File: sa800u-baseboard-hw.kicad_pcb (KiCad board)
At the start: 2 copper layers, 100 x 68 mm, 169 parts, among them IC1 TPS2378DDA, J1 WE-RJ45_7499111121A, J10 2908-05WB-MG, J11 MC-HVT1-S04-G, J12 MC-HVT1-S04-G, J13 MC-HVT1-S04-G, J14 MC-HVT1-S04-G, J2 46756-1001, J4 WE_632723300011, J5 WE_632723300011, J6 WE_632723300011, J7 3-84952-0, J8 F52R-1A7H1-11020, J9 WE_68715014522, Q1 2N7000, Q2 2N7000, Q3 2N7000, T1 749020010A, U1 RTL8111H, U10 MDT580M01001, U11 AP62301Z6-7, U12 AP62301Z6-7, U13 TPS65982BB, U2 LT9611, U3 TXB0104RUT, U4 TXS0102YZPR, U5 TS3USB30EDGSR, U6 FT2232HL-REEL, U7 USB57442G, U8 SA800U-WF, U9 MAX13042EEBC+T, Y1 ECS-1618-250-BN-TR, Y2 ECS-1618-250-BN-TR

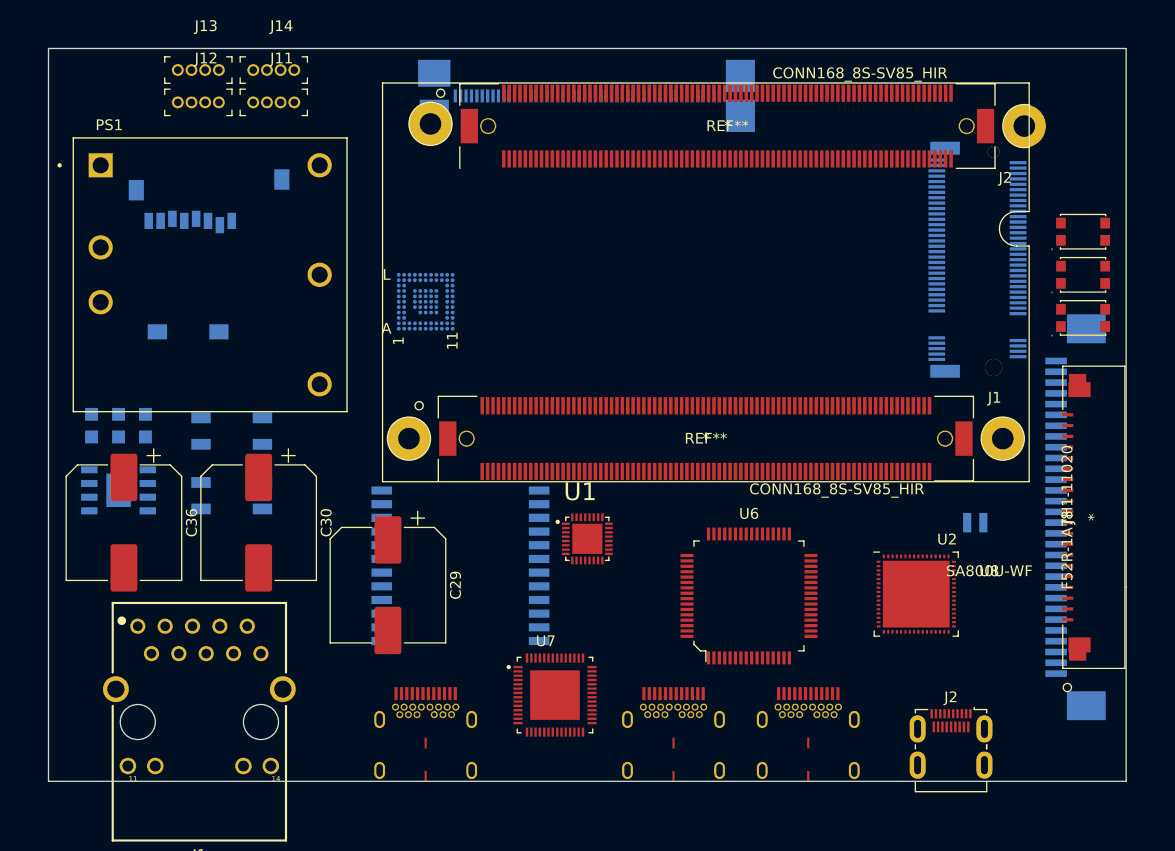
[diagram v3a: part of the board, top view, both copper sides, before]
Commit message: permanently added mounting holes
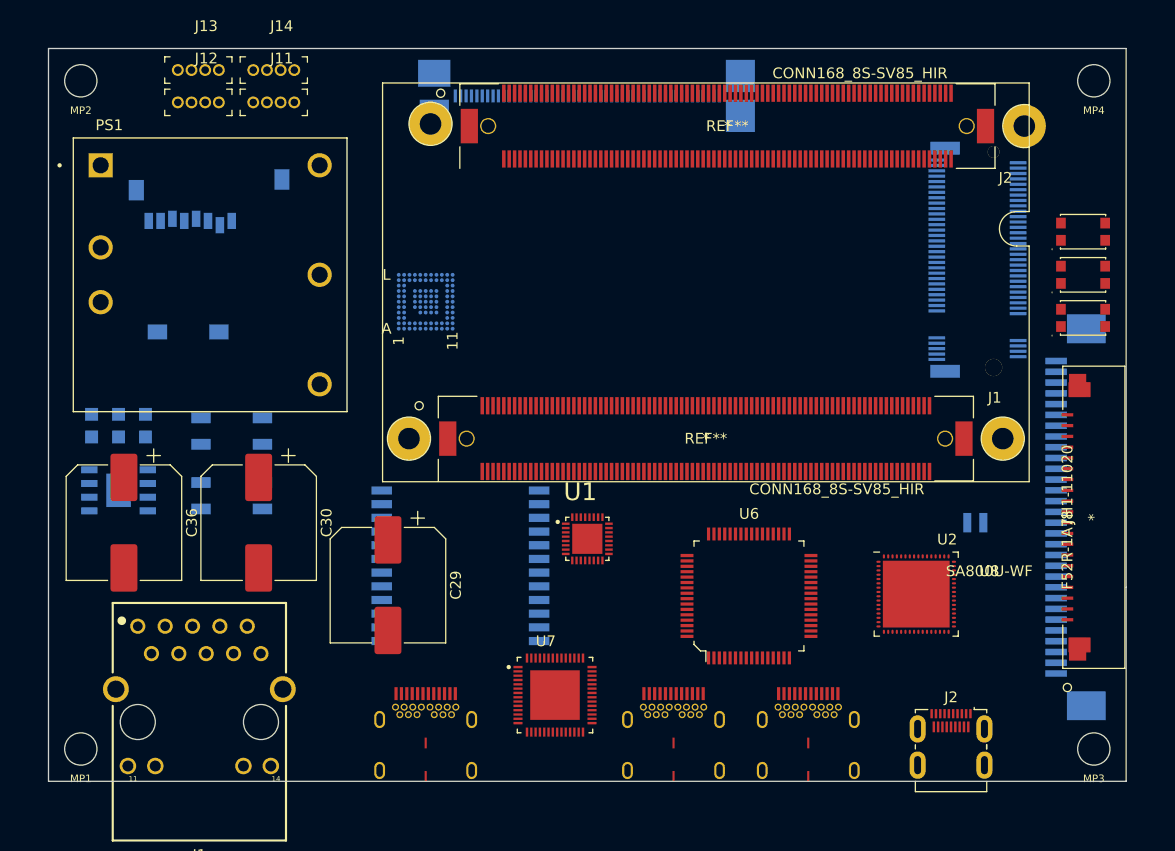
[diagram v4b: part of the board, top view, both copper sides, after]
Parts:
- added MP1: PCB_Mount_Hole_3_NPTH, antmicro-footprints:mounting-hole-3mm-NPTH, F.Cu at (58.0, 147.0)
- added MP2: PCB_Mount_Hole_3_NPTH, antmicro-footprints:mounting-hole-3mm-NPTH, F.Cu at (58.0, 85.0)
- added MP3: PCB_Mount_Hole_3_NPTH, antmicro-footprints:mounting-hole-3mm-NPTH, F.Cu at (152.0, 147.0)
- added MP4: PCB_Mount_Hole_3_NPTH, antmicro-footprints:mounting-hole-3mm-NPTH, F.Cu at (152.0, 85.0)

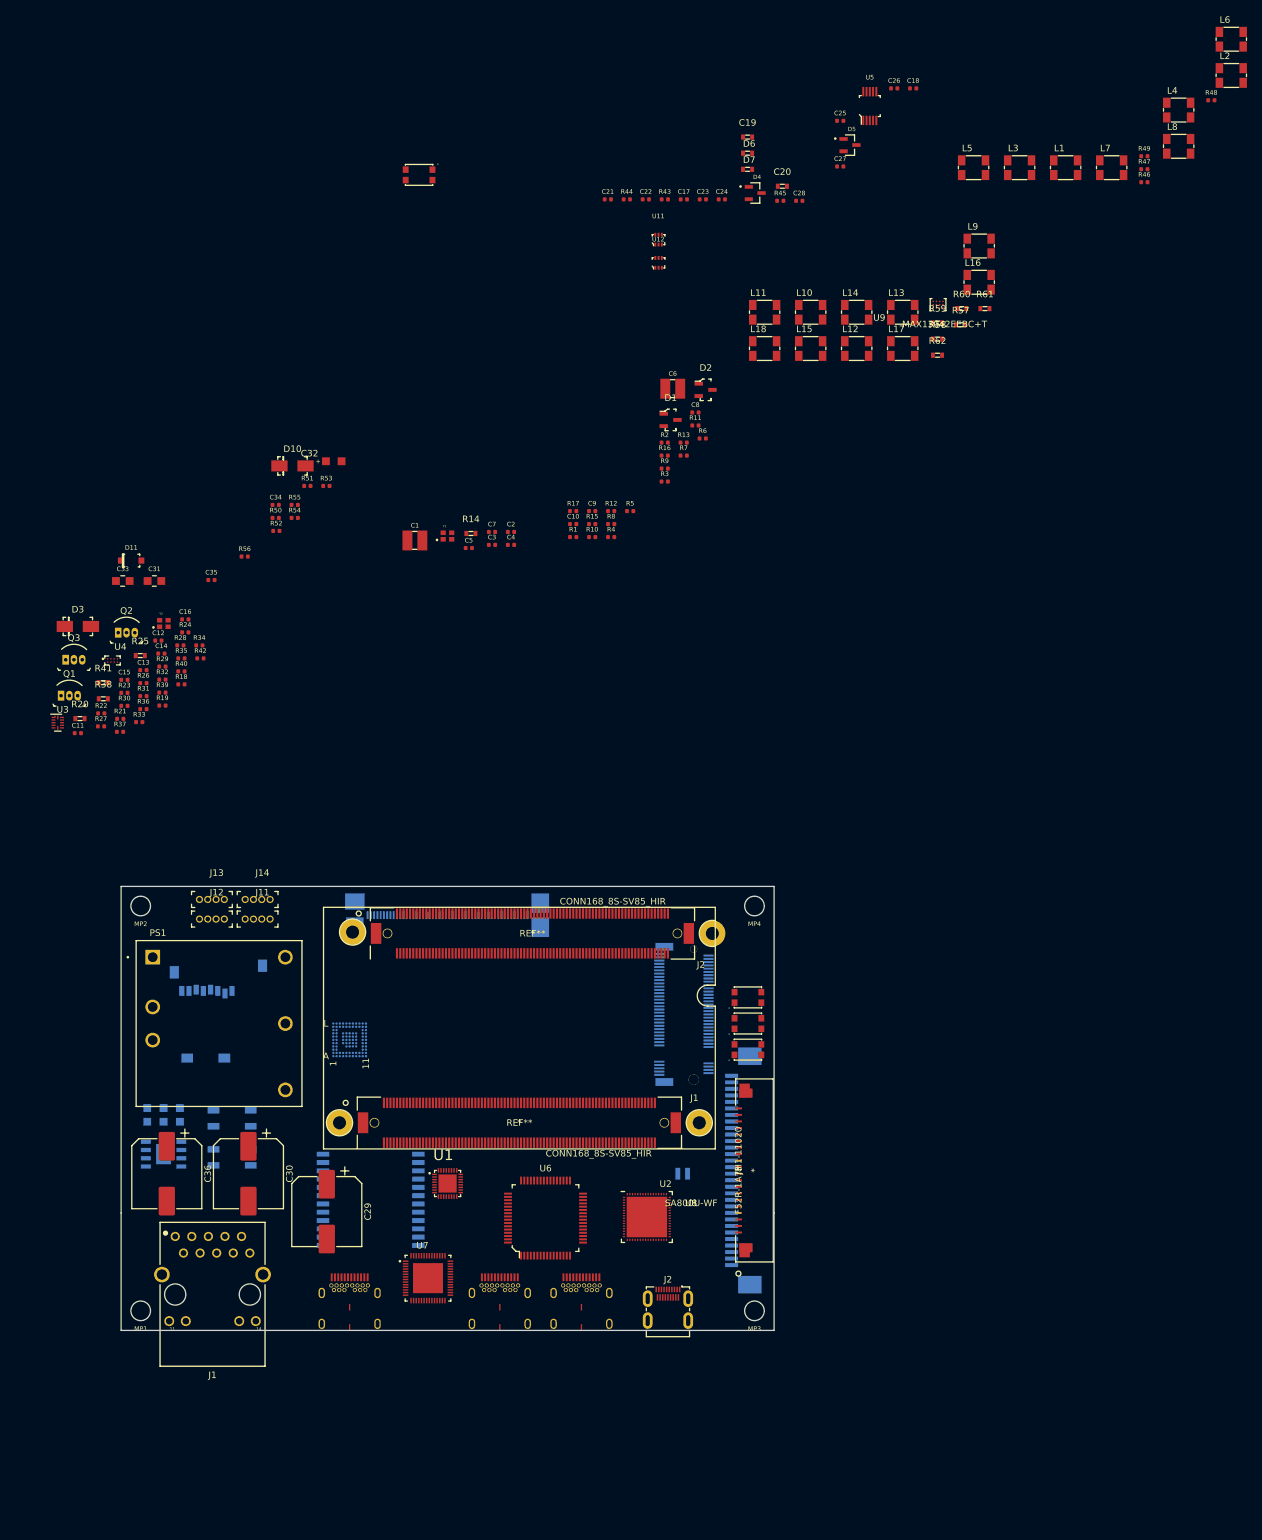
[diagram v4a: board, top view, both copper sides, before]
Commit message: replaced common mode chokes, dedicated for hdmi and with smaller footprint
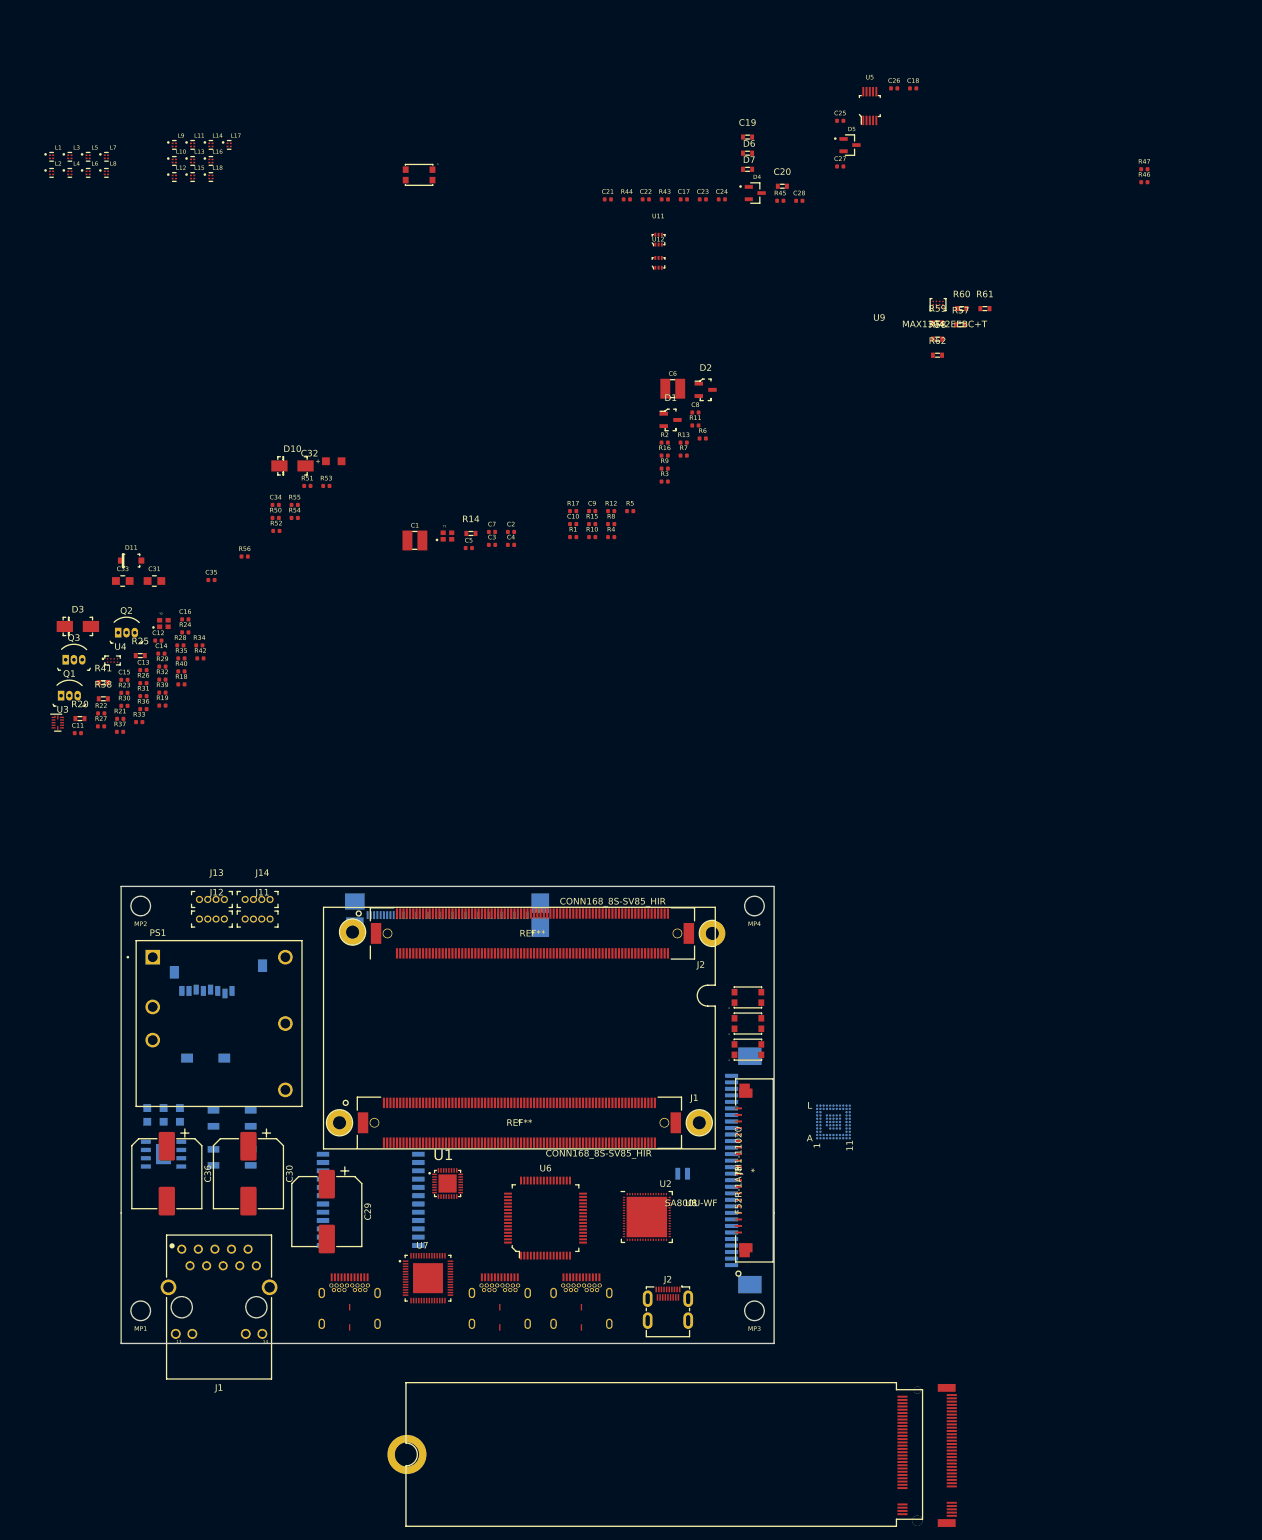
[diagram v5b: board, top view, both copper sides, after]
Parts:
- removed R48, R49: R_4k7_0402, antmicro-footprints:0402-res
- L1, L10, L11, L12, L13, L14, L15, L16, L17, L18, L2, L3, L4, L5, L6, L7, L8, L9: value 744235900 -> NFP0QHB242HS2D; footprint antmicro-footprints:744235900 -> antmicro-footprints:FIL_NFP0QHB242HS2D
- U10: moved to F.Cu
- U13: footprint temp:TPS65982ABZBHR -> USBPD:TPS65982ABZBHR
- moved L2 181.3 mm to (44.4, -27.3)
- moved L6 176.3 mm to (50.0, -27.3)
- moved L4 170.1 mm to (47.2, -27.3)
- moved L8 164.2 mm to (52.8, -27.3)
- moved L1 155.3 mm to (44.4, -29.7)
- moved L7 153.9 mm to (52.8, -29.7)
- moved L3 145.4 mm to (47.2, -29.7)
- moved L5 135.6 mm to (50.0, -29.7)
- moved L9 124.2 mm to (63.2, -31.6)
- moved L16 119.1 mm to (68.8, -29.1)
- moved L13 111.2 mm to (66.0, -29.1)
- moved L17 107.7 mm to (71.6, -31.6)
- moved L12 107.7 mm to (63.2, -26.6)
- moved L14 102.1 mm to (68.8, -31.6)
- moved L10 100.1 mm to (63.2, -29.1)
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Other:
- board size 100 x 68 mm -> 100 x 70 mm

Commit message: modified layout of the board so that ethernet is further away from poe psu
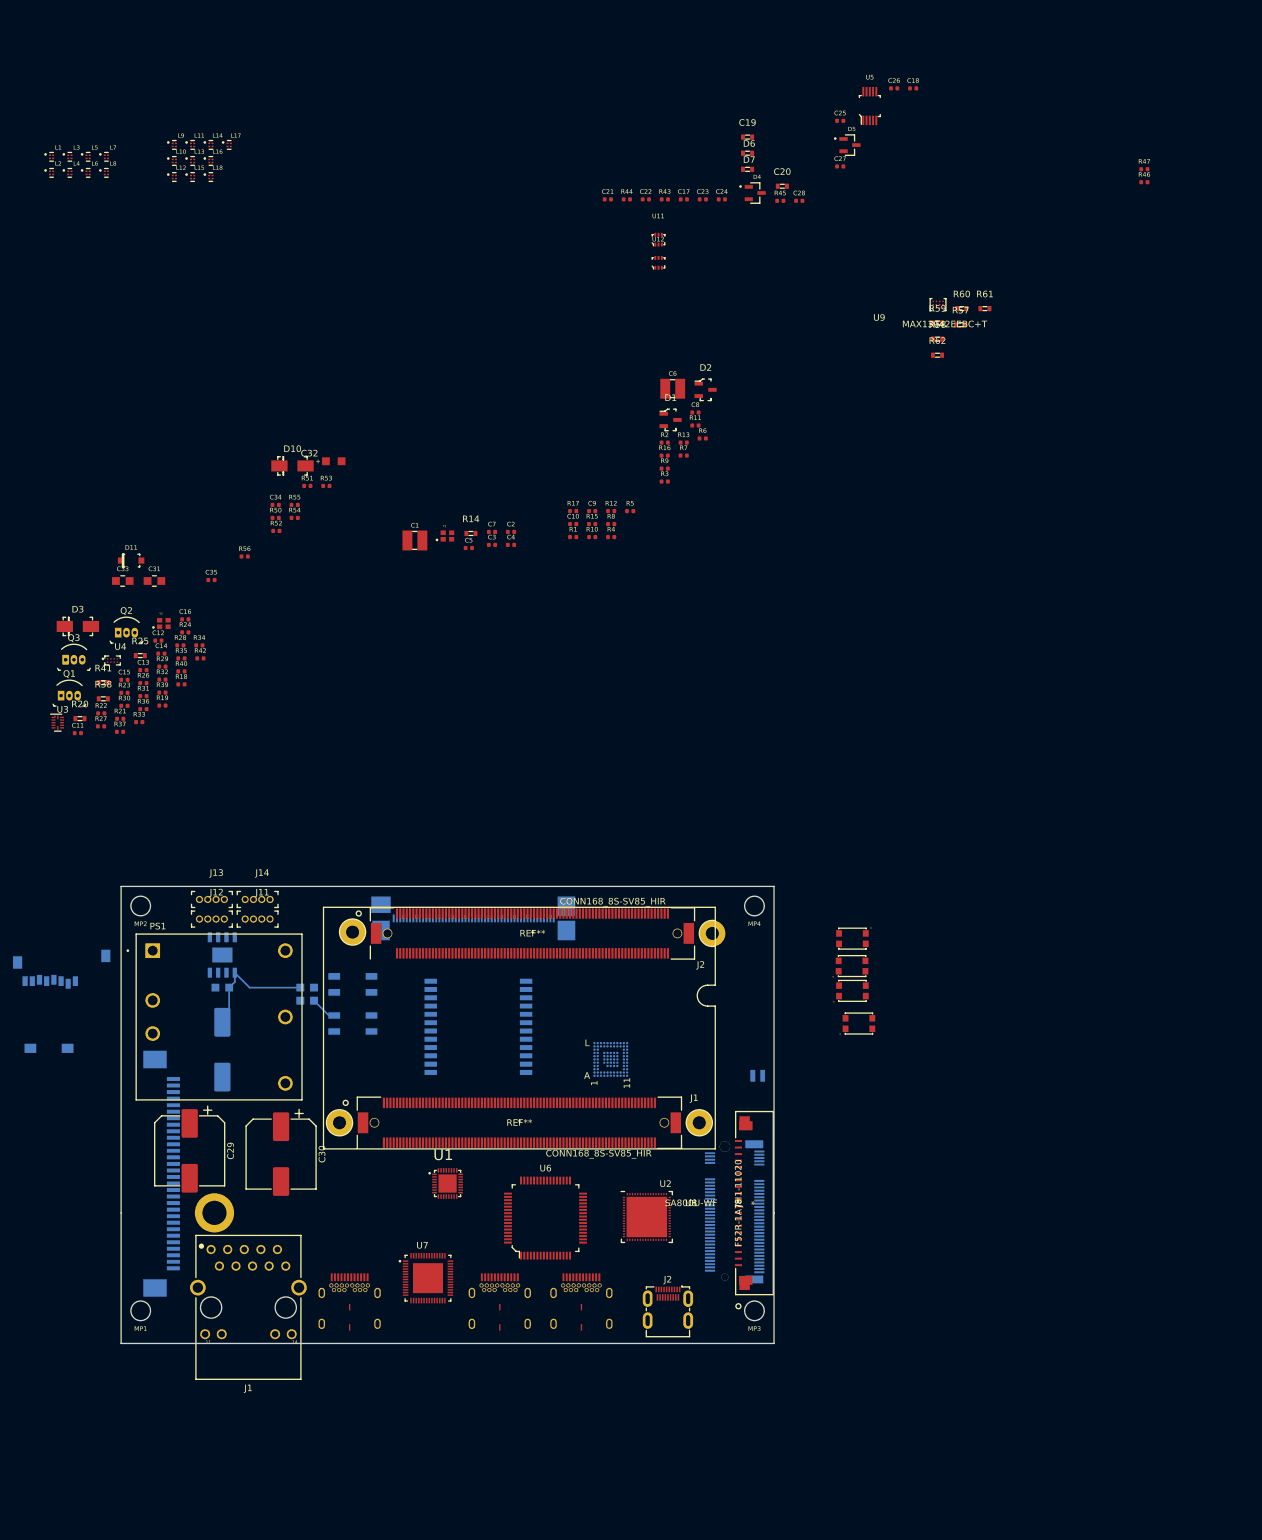
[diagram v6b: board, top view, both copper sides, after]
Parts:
- C36, U10: moved to B.Cu
- moved S1 134.5 mm to (167.0, 90.0)
- moved J7 85.5 mm to (63.0, 126.0), turned to 90 degrees
- moved U13 35.4 mm to (130.0, 108.5)
- moved U10 33.1 mm to (69.0, 143.0)
- moved IC1 31.8 mm to (70.5, 92.5), turned to 90 degrees
- moved T1 31.2 mm to (109.5, 103.5)
- moved FB2 29.4 mm to (83.5, 97.5), turned to 180 degrees
- moved D8 27.6 mm to (90.5, 103.0)
- moved D9 27.6 mm to (90.5, 97.0)
- moved FB3 26.2 mm to (83.5, 99.5), turned to 180 degrees
- moved J10 24.0 mm to (48.0, 96.5)
- moved C29 23.0 mm to (65.5, 122.5)
- moved FB1 22.6 mm to (70.5, 97.5), turned to 180 degrees
- moved C36 20.8 mm to (70.5, 107.0)
- moved BAT1 18.9 mm to (152.5, 111.0)
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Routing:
- net /PoE/VDD: track 0.00 -> 19.4 mm
- net Net-(D8-Pad2): track 0.00 -> 4.04 mm

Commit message: minor fixes
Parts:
- moved J10 95.6 mm to (143.5, 100.0)
- moved S3 17.2 mm to (151.0, 105.5)
- moved S1 16.4 mm to (151.0, 93.5)
- moved S4 16.4 mm to (151.0, 101.5)
- moved S2 16.3 mm to (151.0, 97.5)
- moved U13 7.38 mm to (123.5, 105.0)
- moved J9 5.02 mm to (114.0, 87.0)
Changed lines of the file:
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@@
   )
   (module antmicro-footprints:WE_68715014522 (layer B.Cu)
-    (at 109 87.5)
+    (at 114 87)
     (attr smd)
     (fp_text reference J9 (at -13.9 4.45) (layer B.SilkS)
@@
   )
   (module antmicro-footprints:MicroSD_2908-05WB-MG (layer B.Cu)
-    (at 48 96.5 180)
+    (at 143.5 100 180)
     (attr smd)
     (fp_text reference J10 (at 1.9 5.8) (layer B.SilkS)
@@
   )
   (module antmicro-footprints:SW_SPST_4.2x2.8 (layer F.Cu)
-    (at 167 90)
+    (at 151 93.5)
     (descr KMR211G)
     (tags "SPST Button Switch")
@@
   )
   (module antmicro-footprints:SW_SPST_4.2x2.8 (layer F.Cu)
-    (at 166.95 94.2 180)
+    (at 151 97.5 180)
     (descr KMR211G)
     (tags "SPST Button Switch")
@@
   )
   (module antmicro-footprints:SW_SPST_4.2x2.8 (layer F.Cu)
-    (at 168 103 180)
+    (at 151 105.5 180)
     (descr KMR211G)
     (tags "SPST Button Switch")
@@
   )
   (module antmicro-footprints:SW_SPST_4.2x2.8 (layer F.Cu)
-    (at 167 98 180)
+    (at 151 101.5 180)
     (descr KMR211G)
     (tags "SPST Button Switch")
@@
   )
   (module USBPD:TPS65982ABZBHR (layer B.Cu)
-    (at 130 108.5)
+    (at 123.5 105)
     (fp_text reference U13 (at 0 0) (layer B.SilkS)
       (effects (font (size 1 1) (thickness 0.15)) (justify mirror))
